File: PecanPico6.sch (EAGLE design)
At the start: 62 parts, among them IC1 TPS79718DCKT, IC2 SI4463/4, IC4 LPC1114FHN33/333, IC5 SPV1040, IC6 AS213-92LF, IC7 BMP180, Q2 AP2301

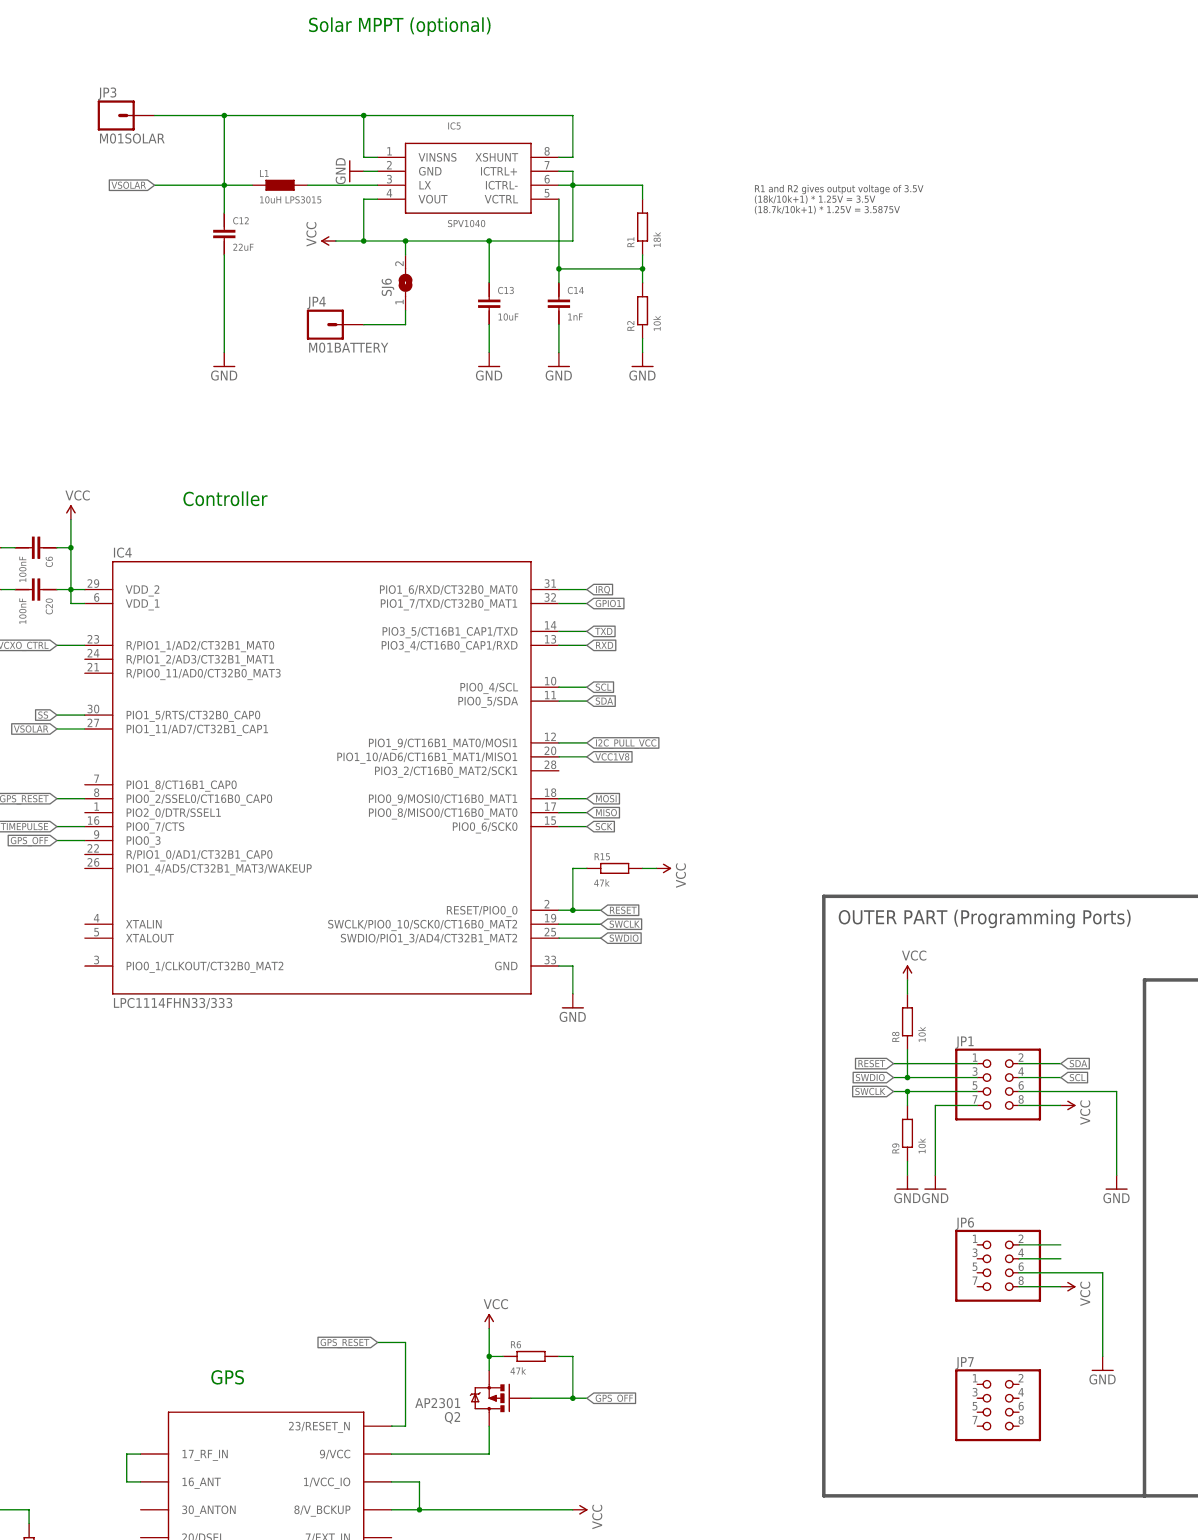
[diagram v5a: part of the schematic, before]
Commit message: Added programmer jumpers
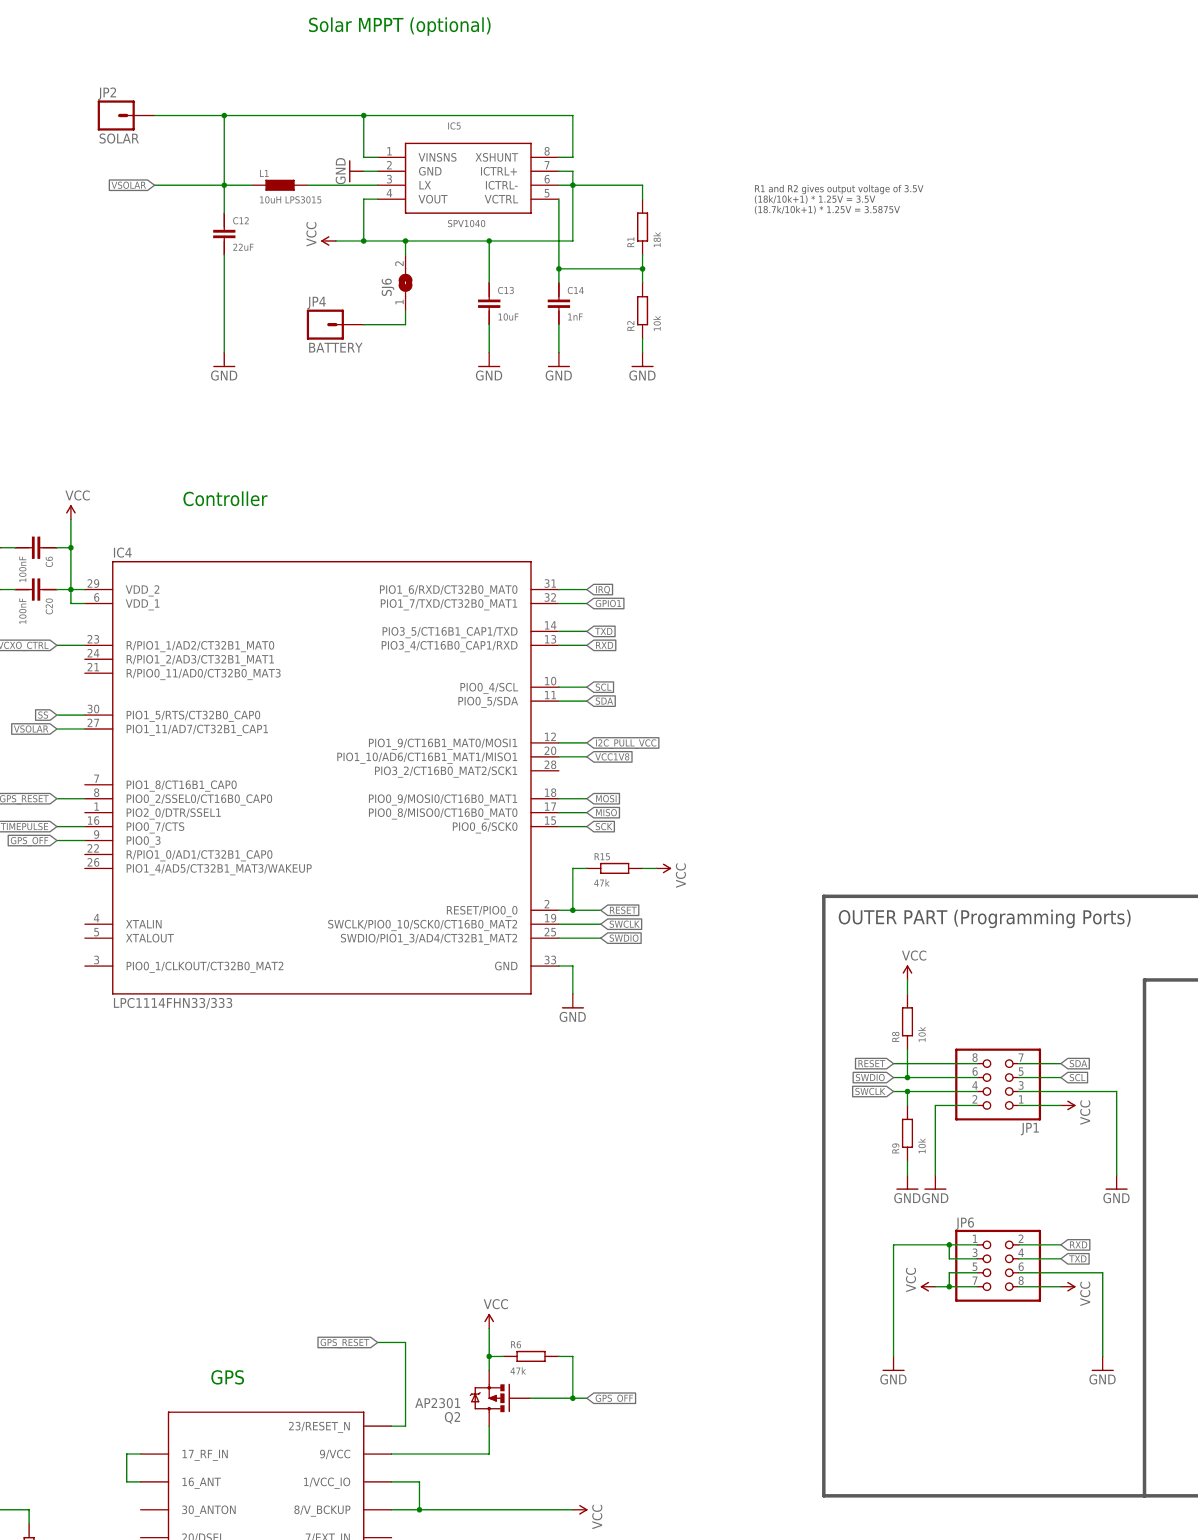
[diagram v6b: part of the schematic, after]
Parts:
- removed JP3: M01SOLAR, sven:M01SOLAR
- removed JP7: (no value), pinhead:PINHD-2X4
- added JP2: SOLAR, sven:M01
- JP4: value M01BATTERY -> BATTERY
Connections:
- net GND: now also JP1.2, JP1.3, JP6.1, JP6.3, JP6.6; no longer JP1.6, JP1.7
- net RESET: now also JP1.8; no longer JP1.1
- net RXD: now also JP6.2
- net SCL: now also JP1.5; no longer JP1.4
- net SDA: now also JP1.7; no longer JP1.2
- net SWCLK: now also JP1.4; no longer JP1.5
- net SWDIO: now also JP1.6; no longer JP1.3
- net TXD: now also JP6.4
- net VCC15: now also JP1.1, JP6.5, JP6.7, JP6.8; no longer JP1.8
- net VSOLAR: now also JP2.1; no longer JP3.1
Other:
- moved on the sheet: JP1
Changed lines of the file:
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@@
 <attribute name="OC_NEWARK" value="unknown"/>
 </part>
-<part name="JP3" library="sven" deviceset="M01" device="SOLAR"/>
-<part name="JP4" library="sven" deviceset="M01" device="BATTERY"/>
+<part name="JP4" library="sven" deviceset="M01" device="BATTERY" value="BATTERY"/>
 <part name="P+15" library="SparkFun" deviceset="3.3V" device="" value="VCC"/>
-<part name="JP1" library="pinhead" deviceset="PINHD-2X4" device=""/>
 <part name="JP6" library="pinhead" deviceset="PINHD-2X4" device=""/>
-<part name="JP7" library="pinhead" deviceset="PINHD-2X4" device=""/>
 <part name="C22" library="sven" deviceset="CAP-0402" device="" value="100pF"/>
 <part name="GND2" library="SparkFun" deviceset="GND" device=""/>
@@
 <part name="P+6" library="SparkFun" deviceset="3.3V" device="" value="VCC"/>
 <part name="GND6" library="SparkFun" deviceset="GND" device=""/>
+<part name="JP2" library="sven" deviceset="M01" device="" value="SOLAR"/>
+<part name="JP1" library="pinhead" deviceset="PINHD-2X4" device=""/>
+<part name="P+11" library="SparkFun" deviceset="3.3V" device="" value="VCC"/>
+<part name="GND14" library="SparkFun" deviceset="GND" device=""/>
 </parts>
 <sheets>
@@
 <attribute name="MPN" x="350.52" y="292.1" size="1.778" layer="96" rot="R90" display="off"/>
 </instance>
-<instance part="JP3" gate="G$1" x="297.18" y="322.58"/>
 <instance part="JP4" gate="G$1" x="335.28" y="284.48"/>
 <instance part="P+15" gate="G$1" x="111.76" y="287.02"/>
-<instance part="JP1" gate="A" x="457.2" y="144.78"/>
 <instance part="JP6" gate="A" x="457.2" y="111.76"/>
-<instance part="JP7" gate="A" x="457.2" y="86.36"/>
 <instance part="C22" gate="G$1" x="208.28" y="170.18"/>
 <instance part="GND2" gate="1" x="170.18" y="182.88"/>
@@
 <instance part="P+6" gate="G$1" x="469.9" y="142.24" rot="R270"/>
 <instance part="GND6" gate="1" x="480.06" y="127"/>
+<instance part="JP2" gate="G$1" x="297.18" y="322.58"/>
+<instance part="JP1" gate="A" x="459.74" y="147.32" rot="R180"/>
+<instance part="P+11" gate="G$1" x="447.04" y="109.22" rot="R90"/>
+<instance part="GND14" gate="1" x="439.42" y="93.98"/>
 </instances>
 <busses>
@@
 <wire x1="447.04" y1="142.24" x2="454.66" y2="142.24" width="0.1524" layer="91"/>
 <pinref part="GND7" gate="1" pin="GND"/>
-<pinref part="JP1" gate="A" pin="7"/>
+<pinref part="JP1" gate="A" pin="2"/>
 </segment>
 <segment>
@@
 <segment>
 <wire x1="462.28" y1="111.76" x2="477.52" y2="111.76" width="0.1524" layer="91"/>
+<pinref part="JP6" gate="A" pin="6"/>
 </segment>
 <segment>
@@
 </segment>
 <segment>
-<pinref part="JP1" gate="A" pin="6"/>
 <wire x1="462.28" y1="144.78" x2="480.06" y2="144.78" width="0.1524" layer="91"/>
 <wire x1="480.06" y1="144.78" x2="480.06" y2="129.54" width="0.1524" layer="91"/>
 <pinref part="GND6" gate="1" pin="GND"/>
+<pinref part="JP1" gate="A" pin="3"/>
+</segment>
+<segment>
+<pinref part="JP6" gate="A" pin="3"/>
+<wire x1="454.66" y1="114.3" x2="449.58" y2="114.3" width="0.1524" layer="91"/>
+<wire x1="449.58" y1="114.3" x2="449.58" y2="116.84" width="0.1524" layer="91"/>
+<pinref part="JP6" gate="A" pin="1"/>
+<wire x1="449.58" y1="116.84" x2="454.66" y2="116.84" width="0.1524" layer="91"/>
+<wire x1="449.58" y1="116.84" x2="439.42" y2="116.84" width="0.1524" layer="91"/>
+<junction x="449.58" y="116.84"/>
+<wire x1="439.42" y1="116.84" x2="439.42" y2="96.52" width="0.1524" layer="91"/>
+<pinref part="GND14" gate="1" pin="GND"/>
 </segment>
 </net>
@@
 <wire x1="462.28" y1="109.22" x2="469.9" y2="109.22" width="0.1524" layer="91"/>
 <pinref part="P+8" gate="G$1" pin="3.3V"/>
-</segment>
-<segment>
-<pinref part="JP1" gate="A" pin="8"/>
+<pinref part="JP6" gate="A" pin="8"/>
+</segment>
+<segment>
 <wire x1="462.28" y1="142.24" x2="469.9" y2="142.24" width="0.1524" layer="91"/>
 <pinref part="P+6" gate="G$1" pin="3.3V"/>
+<pinref part="JP1" gate="A" pin="1"/>
+</segment>
+<segment>
+<pinref part="JP6" gate="A" pin="7"/>
+<wire x1="454.66" y1="109.22" x2="449.58" y2="109.22" width="0.1524" layer="91"/>
+<pinref part="JP6" gate="A" pin="5"/>
+<wire x1="449.58" y1="109.22" x2="447.04" y2="109.22" width="0.1524" layer="91"/>
+<wire x1="454.66" y1="111.76" x2="449.58" y2="111.76" width="0.1524" layer="91"/>
+<wire x1="449.58" y1="111.76" x2="449.58" y2="109.22" width="0.1524" layer="91"/>
+<junction x="449.58" y="109.22"/>
+<pinref part="P+11" gate="G$1" pin="3.3V"/>
 </segment>
 </net>
@@
 </segment>
 <segment>
-<wire x1="462.28" y1="116.84" x2="469.9" y2="116.84" width="0.1524" layer="91"/>
-</segment>
-<segment>
-<pinref part="JP1" gate="A" pin="2"/>
 <wire x1="462.28" y1="149.86" x2="469.9" y2="149.86" width="0.1524" layer="91"/>
 <label x="469.9" y="149.86" size="1.27" layer="95" xref="yes"/>
+<pinref part="JP1" gate="A" pin="7"/>
 </segment>
 </net>
@@
 </segment>
 <segment>
-<wire x1="462.28" y1="114.3" x2="469.9" y2="114.3" width="0.1524" layer="91"/>
-</segment>
-<segment>
-<pinref part="JP1" gate="A" pin="4"/>
 <wire x1="462.28" y1="147.32" x2="469.9" y2="147.32" width="0.1524" layer="91"/>
 <label x="469.9" y="147.32" size="1.27" layer="95" xref="yes"/>
+<pinref part="JP1" gate="A" pin="5"/>
 </segment>
 </net>
@@
 <pinref part="L1" gate="G$1" pin="1"/>
 <pinref part="C12" gate="G$1" pin="2"/>
-<pinref part="JP3" gate="G$1" pin="1"/>
+<pinref part="JP2" gate="G$1" pin="1"/>
 </segment>
 <segment>
@@
 <wire x1="454.66" y1="149.86" x2="439.42" y2="149.86" width="0.1524" layer="91"/>
 <label x="439.42" y="149.86" size="1.27" layer="95" rot="R180" xref="yes"/>
-<pinref part="JP1" gate="A" pin="1"/>
+<pinref part="JP1" gate="A" pin="8"/>
 </segment>
 </net>
@@
 <junction x="441.96" y="147.32"/>
 <pinref part="R8" gate="G$1" pin="1"/>
-<pinref part="JP1" gate="A" pin="3"/>
+<pinref part="JP1" gate="A" pin="6"/>
 </segment>
 </net>
@@
 <junction x="441.96" y="144.78"/>
 <pinref part="R9" gate="G$1" pin="2"/>
-<pinref part="JP1" gate="A" pin="5"/>
+<pinref part="JP1" gate="A" pin="4"/>
 </segment>
 </net>
@@
 <label x="383.54" y="228.6" size="1.27" layer="95" xref="yes"/>
 </segment>
+<segment>
+<wire x1="462.28" y1="114.3" x2="469.9" y2="114.3" width="0.1524" layer="91"/>
+<label x="469.9" y="114.3" size="1.27" layer="95" xref="yes"/>
+<pinref part="JP6" gate="A" pin="4"/>
+</segment>
 </net>
 <net name="RXD" class="0">
@@
 <label x="383.54" y="226.06" size="1.27" layer="95" xref="yes"/>
 </segment>
-</net>
+<segment>
+<wire x1="462.28" y1="116.84" x2="469.9" y2="116.84" width="0.1524" layer="91"/>
+<label x="469.9" y="116.84" size="1.27" layer="95" xref="yes"/>
+<pinref part="JP6" gate="A" pin="2"/>
+</segment>
+</net>
